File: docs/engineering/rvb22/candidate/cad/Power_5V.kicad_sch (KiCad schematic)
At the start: 23 parts, among them U121 LM5164DDAR

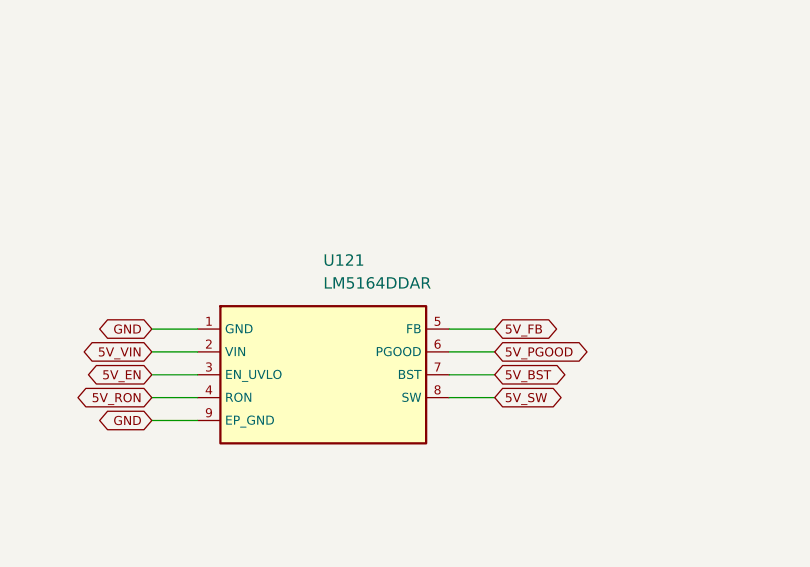
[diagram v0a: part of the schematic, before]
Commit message: I28: automotive-qualify 5V buck and document power signoff
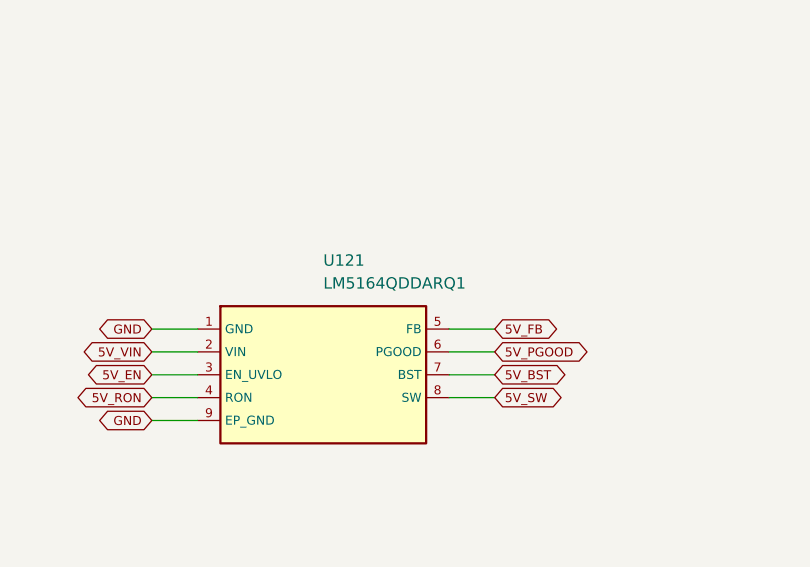
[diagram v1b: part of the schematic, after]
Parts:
- U121: value LM5164DDAR -> LM5164QDDARQ1; symbol RevB:LM5164DDAR -> RevB:LM5164QDDARQ1; LCSC C477928 -> C2072225; MPN LM5164DDAR -> LM5164QDDARQ1
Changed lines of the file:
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@@
 (wire (pts (xy 95.25 91.44) (xy 90.17 91.44)) (stroke (width 0) (type default)))
 (global_label "GND" (shape bidirectional) (at 90.17 91.44 180) (effects (font (size 1.0 1.0)) (justify right)) (property "Intersheetrefs" "${INTERSHEET_REFS}" (at 90.17 91.44 0) (effects (font (size 1.27 1.27)) (justify left) hide)))
-(symbol (lib_id "RevB:LM5164DDAR") (at 109.22 86.36 0) (unit 1) (in_bom yes) (on_board yes) (dnp no) (property "Reference" "U121" (at 109.22 73.66 0) (effects (font (size 1.27 1.27)) (justify left))) (property "Value" "LM5164DDAR" (at 109.22 76.2 0) (effects (font (size 1.27 1.27)) (justify left))) (property "Footprint" "RevB:TI_DDA0008B_4214849B" (at 0 0 0) (effects (font (size 1.27 1.27)) (justify left) hide)) (property "Datasheet" "https://www.ti.com/lit/ds/symlink/lm5164.pdf" (at 0 0 0) (effects (font (size 1.27 1.27)) (justify left) hide)) (property "MPN" "LM5164DDAR" (at 0 0 0) (effects (font (size 1.27 1.27)) (justify left) hide)) (property "Qualification" "VERIFIED component selection; qualification/productization/SELECTED_COMPONENTS.json; physical acceptance separate" (at 0 0 0) (effects (font (size 1.27 1.27)) (justify left) hide)) (pin "1") (pin "2") (pin "3") (pin "4") (pin "5") (pin "6") (pin "7") (pin "8") (pin "9") (instances (project "GR86_CCA_RevB" (path "/4108b523-946e-532e-b734-a3b8d9b0fa0b/6003342a-9143-57b0-8e3d-d4df9582200f" (reference "U121") (unit 1)))) (property "LCSC" "C477928" (at 0 0 0) (effects (font (size 1.27 1.27)) (hide yes))) (property "Manufacturer" "Texas Instruments" (at 0 0 0) (effects (font (size 1.27 1.27)) (hide yes))) (property "Assembly" "FACTORY" (at 0 0 0) (effects (font (size 1.27 1.27)) (hide yes))))
+(symbol (lib_id "RevB:LM5164QDDARQ1") (at 109.22 86.36 0) (unit 1) (in_bom yes) (on_board yes) (dnp no) (property "Reference" "U121" (at 109.22 73.66 0) (effects (font (size 1.27 1.27)) (justify left))) (property "Value" "LM5164QDDARQ1" (at 109.22 76.2 0) (effects (font (size 1.27 1.27)) (justify left))) (property "Footprint" "RevB:TI_DDA0008B_4214849B" (at 0 0 0) (effects (font (size 1.27 1.27)) (justify left) hide)) (property "Datasheet" "https://www.ti.com/lit/ds/symlink/lm5164-q1.pdf" (at 0 0 0) (effects (font (size 1.27 1.27)) (justify left) hide)) (property "MPN" "LM5164QDDARQ1" (at 0 0 0) (effects (font (size 1.27 1.27)) (justify left) hide)) (property "Qualification" "VERIFIED component selection; qualification/productization/SELECTED_COMPONENTS.json; physical acceptance separate" (at 0 0 0) (effects (font (size 1.27 1.27)) (justify left) hide)) (pin "1") (pin "2") (pin "3") (pin "4") (pin "5") (pin "6") (pin "7") (pin "8") (pin "9") (instances (project "GR86_CCA_RevB" (path "/4108b523-946e-532e-b734-a3b8d9b0fa0b/6003342a-9143-57b0-8e3d-d4df9582200f" (reference "U121") (unit 1)))) (property "LCSC" "C2072225" (at 0 0 0) (effects (font (size 1.27 1.27)) (hide yes))) (property "Manufacturer" "Texas Instruments" (at 0 0 0) (effects (font (size 1.27 1.27)) (hide yes))) (property "Assembly" "FACTORY" (at 0 0 0) (effects (font (size 1.27 1.27)) (hide yes))))
 (wire (pts (xy 35.56 72.39) (xy 35.56 67.31)) (stroke (width 0) (type default)))
 (global_label "5V_VIN" (shape bidirectional) (at 35.56 67.31 0) (effects (font (size 1.0 1.0)) (justify left)) (property "Intersheetrefs" "${INTERSHEET_REFS}" (at 35.56 67.31 0) (effects (font (size 1.27 1.27)) (justify left) hide)))

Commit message: I28: retain qualified LM5164 symbol identity for Q1 fitted variant
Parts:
- U121: symbol RevB:LM5164QDDARQ1 -> RevB:LM5164DDAR
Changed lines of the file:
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@@
 (wire (pts (xy 95.25 91.44) (xy 90.17 91.44)) (stroke (width 0) (type default)))
 (global_label "GND" (shape bidirectional) (at 90.17 91.44 180) (effects (font (size 1.0 1.0)) (justify right)) (property "Intersheetrefs" "${INTERSHEET_REFS}" (at 90.17 91.44 0) (effects (font (size 1.27 1.27)) (justify left) hide)))
-(symbol (lib_id "RevB:LM5164QDDARQ1") (at 109.22 86.36 0) (unit 1) (in_bom yes) (on_board yes) (dnp no) (property "Reference" "U121" (at 109.22 73.66 0) (effects (font (size 1.27 1.27)) (justify left))) (property "Value" "LM5164QDDARQ1" (at 109.22 76.2 0) (effects (font (size 1.27 1.27)) (justify left))) (property "Footprint" "RevB:TI_DDA0008B_4214849B" (at 0 0 0) (effects (font (size 1.27 1.27)) (justify left) hide)) (property "Datasheet" "https://www.ti.com/lit/ds/symlink/lm5164-q1.pdf" (at 0 0 0) (effects (font (size 1.27 1.27)) (justify left) hide)) (property "MPN" "LM5164QDDARQ1" (at 0 0 0) (effects (font (size 1.27 1.27)) (justify left) hide)) (property "Qualification" "VERIFIED component selection; qualification/productization/SELECTED_COMPONENTS.json; physical acceptance separate" (at 0 0 0) (effects (font (size 1.27 1.27)) (justify left) hide)) (pin "1") (pin "2") (pin "3") (pin "4") (pin "5") (pin "6") (pin "7") (pin "8") (pin "9") (instances (project "GR86_CCA_RevB" (path "/4108b523-946e-532e-b734-a3b8d9b0fa0b/6003342a-9143-57b0-8e3d-d4df9582200f" (reference "U121") (unit 1)))) (property "LCSC" "C2072225" (at 0 0 0) (effects (font (size 1.27 1.27)) (hide yes))) (property "Manufacturer" "Texas Instruments" (at 0 0 0) (effects (font (size 1.27 1.27)) (hide yes))) (property "Assembly" "FACTORY" (at 0 0 0) (effects (font (size 1.27 1.27)) (hide yes))))
+(symbol (lib_id "RevB:LM5164DDAR") (at 109.22 86.36 0) (unit 1) (in_bom yes) (on_board yes) (dnp no) (property "Reference" "U121" (at 109.22 73.66 0) (effects (font (size 1.27 1.27)) (justify left))) (property "Value" "LM5164QDDARQ1" (at 109.22 76.2 0) (effects (font (size 1.27 1.27)) (justify left))) (property "Footprint" "RevB:TI_DDA0008B_4214849B" (at 0 0 0) (effects (font (size 1.27 1.27)) (justify left) hide)) (property "Datasheet" "https://www.ti.com/lit/ds/symlink/lm5164-q1.pdf" (at 0 0 0) (effects (font (size 1.27 1.27)) (justify left) hide)) (property "MPN" "LM5164QDDARQ1" (at 0 0 0) (effects (font (size 1.27 1.27)) (justify left) hide)) (property "Qualification" "VERIFIED component selection; qualification/productization/SELECTED_COMPONENTS.json; physical acceptance separate" (at 0 0 0) (effects (font (size 1.27 1.27)) (justify left) hide)) (pin "1") (pin "2") (pin "3") (pin "4") (pin "5") (pin "6") (pin "7") (pin "8") (pin "9") (instances (project "GR86_CCA_RevB" (path "/4108b523-946e-532e-b734-a3b8d9b0fa0b/6003342a-9143-57b0-8e3d-d4df9582200f" (reference "U121") (unit 1)))) (property "LCSC" "C2072225" (at 0 0 0) (effects (font (size 1.27 1.27)) (hide yes))) (property "Manufacturer" "Texas Instruments" (at 0 0 0) (effects (font (size 1.27 1.27)) (hide yes))) (property "Assembly" "FACTORY" (at 0 0 0) (effects (font (size 1.27 1.27)) (hide yes))))
 (wire (pts (xy 35.56 72.39) (xy 35.56 67.31)) (stroke (width 0) (type default)))
 (global_label "5V_VIN" (shape bidirectional) (at 35.56 67.31 0) (effects (font (size 1.0 1.0)) (justify left)) (property "Intersheetrefs" "${INTERSHEET_REFS}" (at 35.56 67.31 0) (effects (font (size 1.27 1.27)) (justify left) hide)))
